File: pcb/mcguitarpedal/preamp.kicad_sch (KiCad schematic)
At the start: 31 parts, among them J8 POT_HP_VOLUME_10k, U3 LM4562

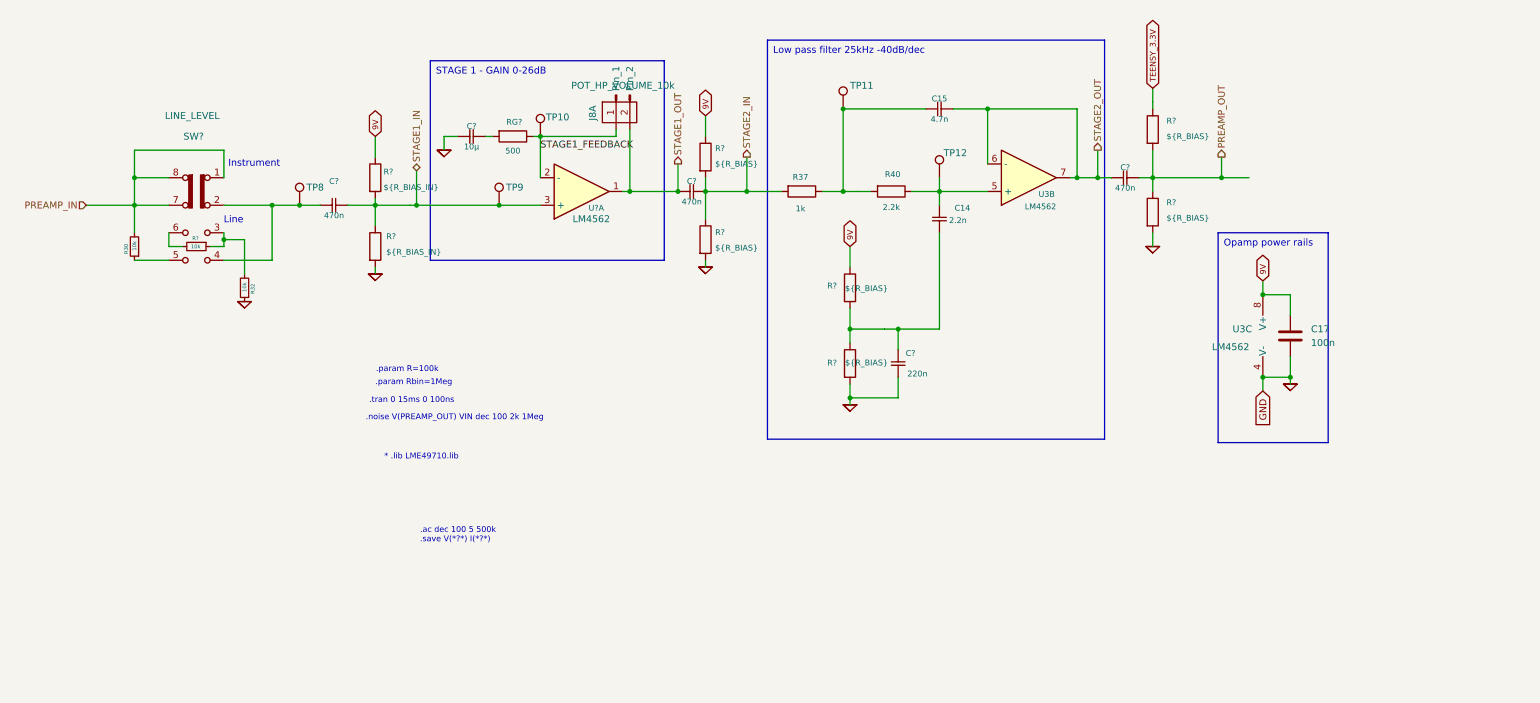
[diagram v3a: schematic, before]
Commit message: Missing models, PCB pdf exports
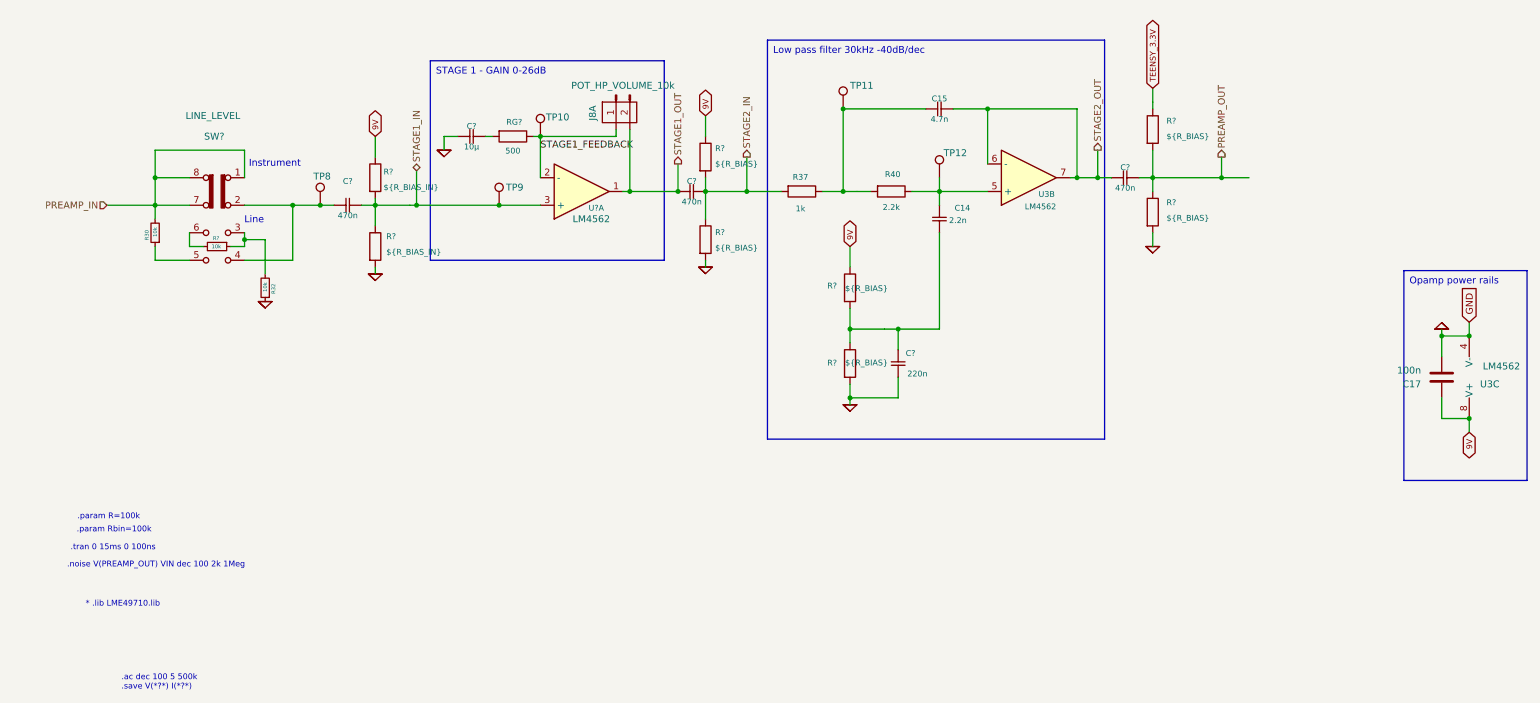
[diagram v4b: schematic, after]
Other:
- note added: ".param Rbin=100k"
- note removed: ".param Rbin=1Meg"
- moved on the sheet: C17, C?, R30, R32, R?, SW?, TP8, U3C
